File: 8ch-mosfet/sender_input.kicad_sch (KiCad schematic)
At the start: 4 parts, among them J16 Conn_01x02

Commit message: component layout looking crispy.
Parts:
- renumbered J16 to INPUT2, R102 to R101, R101 to R102
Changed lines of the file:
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@@
 		(dnp no)
 		(fields_autoplaced yes)
-		(property "Reference" "#PWR096"
+		(property "Reference" "#PWR095"
 			(at 152.4 102.87 0)
 			(effects
@@
 			(project "8ch-mosfet"
 				(path "/c83c6236-96e9-46ad-9d7a-9e2efa4a7966/96edcf10-ad2e-4b0c-9bcf-7ec233542517"
-					(reference "#PWR096")
-					(unit 1)
-				)
-				(path "/c83c6236-96e9-46ad-9d7a-9e2efa4a7966/b7d804d7-e10b-40c8-a6a0-65b4ae1f95ab"
-					(reference "#PWR093")
-					(unit 1)
-				)
-				(path "/c83c6236-96e9-46ad-9d7a-9e2efa4a7966/be792642-71a0-4d31-8160-e0873aa75416"
-					(reference "#PWR0102")
-					(unit 1)
-				)
-				(path "/c83c6236-96e9-46ad-9d7a-9e2efa4a7966/f630e7bf-424c-48d0-b4f5-b992ebe5ac06"
-					(reference "#PWR099")
+					(reference "#PWR095")
+					(unit 1)
+				)
+				(path "/c83c6236-96e9-46ad-9d7a-9e2efa4a7966/b7d804d7-e10b-40c8-a6a0-65b4ae1f95ab"
+					(reference "#PWR092")
+					(unit 1)
+				)
+				(path "/c83c6236-96e9-46ad-9d7a-9e2efa4a7966/be792642-71a0-4d31-8160-e0873aa75416"
+					(reference "#PWR0101")
+					(unit 1)
+				)
+				(path "/c83c6236-96e9-46ad-9d7a-9e2efa4a7966/f630e7bf-424c-48d0-b4f5-b992ebe5ac06"
+					(reference "#PWR098")
 					(unit 1)
 				)
@@
 		(on_board yes)
 		(dnp no)
-		(property "Reference" "#PWR097"
+		(property "Reference" "#PWR096"
 			(at 152.4 125.73 0)
 			(effects
@@
 			(project "8ch-mosfet"
 				(path "/c83c6236-96e9-46ad-9d7a-9e2efa4a7966/96edcf10-ad2e-4b0c-9bcf-7ec233542517"
-					(reference "#PWR097")
-					(unit 1)
-				)
-				(path "/c83c6236-96e9-46ad-9d7a-9e2efa4a7966/b7d804d7-e10b-40c8-a6a0-65b4ae1f95ab"
-					(reference "#PWR094")
-					(unit 1)
-				)
-				(path "/c83c6236-96e9-46ad-9d7a-9e2efa4a7966/be792642-71a0-4d31-8160-e0873aa75416"
-					(reference "#PWR0103")
-					(unit 1)
-				)
-				(path "/c83c6236-96e9-46ad-9d7a-9e2efa4a7966/f630e7bf-424c-48d0-b4f5-b992ebe5ac06"
-					(reference "#PWR0100")
+					(reference "#PWR096")
+					(unit 1)
+				)
+				(path "/c83c6236-96e9-46ad-9d7a-9e2efa4a7966/b7d804d7-e10b-40c8-a6a0-65b4ae1f95ab"
+					(reference "#PWR093")
+					(unit 1)
+				)
+				(path "/c83c6236-96e9-46ad-9d7a-9e2efa4a7966/be792642-71a0-4d31-8160-e0873aa75416"
+					(reference "#PWR0102")
+					(unit 1)
+				)
+				(path "/c83c6236-96e9-46ad-9d7a-9e2efa4a7966/f630e7bf-424c-48d0-b4f5-b992ebe5ac06"
+					(reference "#PWR099")
 					(unit 1)
 				)
@@
 		(dnp no)
 		(fields_autoplaced yes)
-		(property "Reference" "#PWR098"
+		(property "Reference" "#PWR097"
 			(at 162.56 102.87 0)
 			(effects
@@
 			(project "8ch-mosfet"
 				(path "/c83c6236-96e9-46ad-9d7a-9e2efa4a7966/96edcf10-ad2e-4b0c-9bcf-7ec233542517"
-					(reference "#PWR098")
-					(unit 1)
-				)
-				(path "/c83c6236-96e9-46ad-9d7a-9e2efa4a7966/b7d804d7-e10b-40c8-a6a0-65b4ae1f95ab"
-					(reference "#PWR095")
-					(unit 1)
-				)
-				(path "/c83c6236-96e9-46ad-9d7a-9e2efa4a7966/be792642-71a0-4d31-8160-e0873aa75416"
-					(reference "#PWR0104")
-					(unit 1)
-				)
-				(path "/c83c6236-96e9-46ad-9d7a-9e2efa4a7966/f630e7bf-424c-48d0-b4f5-b992ebe5ac06"
-					(reference "#PWR0101")
+					(reference "#PWR097")
+					(unit 1)
+				)
+				(path "/c83c6236-96e9-46ad-9d7a-9e2efa4a7966/b7d804d7-e10b-40c8-a6a0-65b4ae1f95ab"
+					(reference "#PWR094")
+					(unit 1)
+				)
+				(path "/c83c6236-96e9-46ad-9d7a-9e2efa4a7966/be792642-71a0-4d31-8160-e0873aa75416"
+					(reference "#PWR0103")
+					(unit 1)
+				)
+				(path "/c83c6236-96e9-46ad-9d7a-9e2efa4a7966/f630e7bf-424c-48d0-b4f5-b992ebe5ac06"
+					(reference "#PWR0100")
 					(unit 1)
 				)
@@
 		(dnp no)
 		(fields_autoplaced yes)
-		(property "Reference" "J16"
+		(property "Reference" "INPUT2"
 			(at 142.24 100.33 0)
 			(effects
@@
 			(project ""
 				(path "/c83c6236-96e9-46ad-9d7a-9e2efa4a7966/96edcf10-ad2e-4b0c-9bcf-7ec233542517"
-					(reference "J17")
-					(unit 1)
-				)
-				(path "/c83c6236-96e9-46ad-9d7a-9e2efa4a7966/b7d804d7-e10b-40c8-a6a0-65b4ae1f95ab"
-					(reference "J16")
-					(unit 1)
-				)
-				(path "/c83c6236-96e9-46ad-9d7a-9e2efa4a7966/be792642-71a0-4d31-8160-e0873aa75416"
-					(reference "J19")
-					(unit 1)
-				)
-				(path "/c83c6236-96e9-46ad-9d7a-9e2efa4a7966/f630e7bf-424c-48d0-b4f5-b992ebe5ac06"
-					(reference "J18")
+					(reference "INPUT2")
+					(unit 1)
+				)
+				(path "/c83c6236-96e9-46ad-9d7a-9e2efa4a7966/b7d804d7-e10b-40c8-a6a0-65b4ae1f95ab"
+					(reference "INPUT1")
+					(unit 1)
+				)
+				(path "/c83c6236-96e9-46ad-9d7a-9e2efa4a7966/be792642-71a0-4d31-8160-e0873aa75416"
+					(reference "INPUT4")
+					(unit 1)
+				)
+				(path "/c83c6236-96e9-46ad-9d7a-9e2efa4a7966/f630e7bf-424c-48d0-b4f5-b992ebe5ac06"
+					(reference "INPUT3")
 					(unit 1)
 				)
@@
 		(dnp no)
 		(fields_autoplaced yes)
-		(property "Reference" "R102"
+		(property "Reference" "R101"
 			(at 154.94 111.76 0)
 			(effects
@@
 			(project "8ch-mosfet"
 				(path "/c83c6236-96e9-46ad-9d7a-9e2efa4a7966/96edcf10-ad2e-4b0c-9bcf-7ec233542517"
-					(reference "R102")
-					(unit 1)
-				)
-				(path "/c83c6236-96e9-46ad-9d7a-9e2efa4a7966/b7d804d7-e10b-40c8-a6a0-65b4ae1f95ab"
-					(reference "R99")
-					(unit 1)
-				)
-				(path "/c83c6236-96e9-46ad-9d7a-9e2efa4a7966/be792642-71a0-4d31-8160-e0873aa75416"
-					(reference "R108")
-					(unit 1)
-				)
-				(path "/c83c6236-96e9-46ad-9d7a-9e2efa4a7966/f630e7bf-424c-48d0-b4f5-b992ebe5ac06"
-					(reference "R105")
+					(reference "R101")
+					(unit 1)
+				)
+				(path "/c83c6236-96e9-46ad-9d7a-9e2efa4a7966/b7d804d7-e10b-40c8-a6a0-65b4ae1f95ab"
+					(reference "R98")
+					(unit 1)
+				)
+				(path "/c83c6236-96e9-46ad-9d7a-9e2efa4a7966/be792642-71a0-4d31-8160-e0873aa75416"
+					(reference "R107")
+					(unit 1)
+				)
+				(path "/c83c6236-96e9-46ad-9d7a-9e2efa4a7966/f630e7bf-424c-48d0-b4f5-b992ebe5ac06"
+					(reference "R104")
 					(unit 1)
 				)
@@
 		(dnp yes)
 		(fields_autoplaced yes)
-		(property "Reference" "R101"
+		(property "Reference" "R102"
 			(at 165.1 101.6 0)
 			(effects
@@
 			(project "8ch-mosfet"
 				(path "/c83c6236-96e9-46ad-9d7a-9e2efa4a7966/96edcf10-ad2e-4b0c-9bcf-7ec233542517"
-					(reference "R101")
-					(unit 1)
-				)
-				(path "/c83c6236-96e9-46ad-9d7a-9e2efa4a7966/b7d804d7-e10b-40c8-a6a0-65b4ae1f95ab"
-					(reference "R98")
-					(unit 1)
-				)
-				(path "/c83c6236-96e9-46ad-9d7a-9e2efa4a7966/be792642-71a0-4d31-8160-e0873aa75416"
-					(reference "R107")
-					(unit 1)
-				)
-				(path "/c83c6236-96e9-46ad-9d7a-9e2efa4a7966/f630e7bf-424c-48d0-b4f5-b992ebe5ac06"
-					(reference "R104")
-					(unit 1)
-				)
+					(reference "R102")
+					(unit 1)
+				)
+				(path "/c83c6236-96e9-46ad-9d7a-9e2efa4a7966/b7d804d7-e10b-40c8-a6a0-65b4ae1f95ab"
+					(reference "R99")
+					(unit 1)
+				)
+				(path "/c83c6236-96e9-46ad-9d7a-9e2efa4a7966/be792642-71a0-4d31-8160-e0873aa75416"
+					(reference "R108")
+					(unit 1)
+				)
+				(path "/c83c6236-96e9-46ad-9d7a-9e2efa4a7966/f630e7bf-424c-48d0-b4f5-b992ebe5ac06"
+					(reference "R105")
+					(unit 1)
+				)

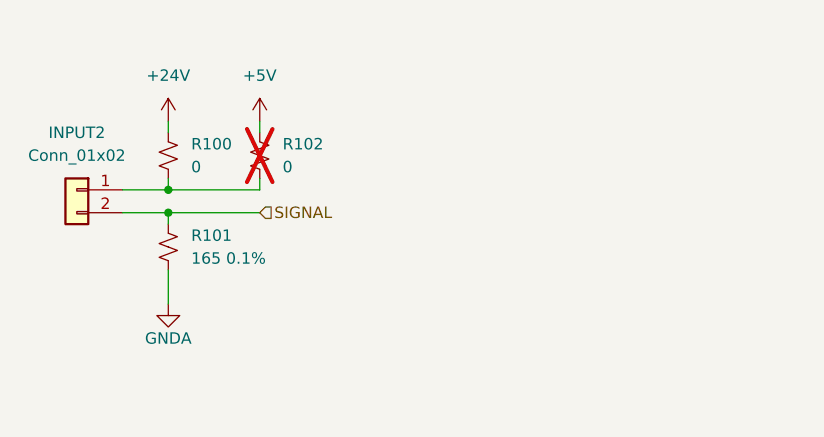
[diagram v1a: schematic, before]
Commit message: i think i figured out the tank sensors?
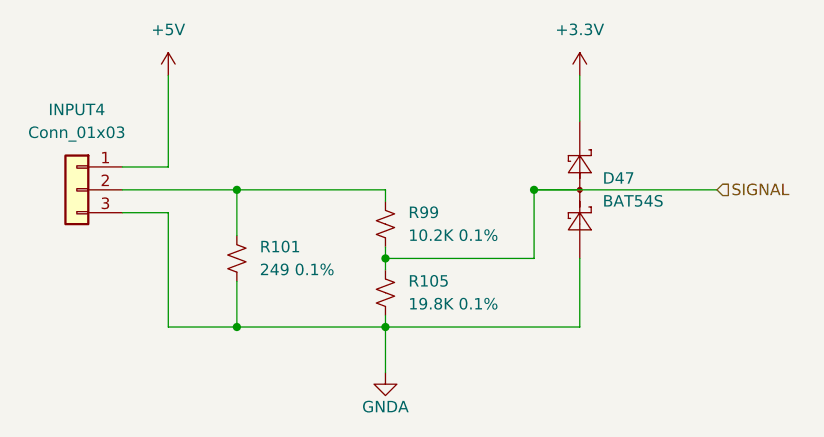
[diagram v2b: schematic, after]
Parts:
- removed INPUT2: Conn_01x02, Connector_JST:JST_PH_B2B-PH-K_1x02_P2.00mm_Vertical, symbol Connector_Generic:Conn_01x02
- removed R100, R102: 0, Resistor_SMD:R_0805_2012Metric_Pad1.20x1.40mm_HandSolder, symbol Device:R_Small_US
- added D47: BAT54S, Package_TO_SOT_SMD:SOT-23, symbol Diode:BAT54S
- added INPUT4: Conn_01x03, Connector_JST:JST_PH_B3B-PH-K_1x03_P2.00mm_Vertical, symbol Connector_Generic:Conn_01x03
- added R105: 19.8K 0.1%, Resistor_SMD:R_0805_2012Metric_Pad1.20x1.40mm_HandSolder, symbol Device:R_Small_US
- added R99: 10.2K 0.1%, Resistor_SMD:R_0805_2012Metric_Pad1.20x1.40mm_HandSolder, symbol Device:R_Small_US
- R101: value 165 0.1% -> 249 0.1%
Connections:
- net +5V: now also INPUT4.1 (Pin_1)
- net GNDA: now also D47.1 (A), INPUT4.3 (Pin_3), R105.1
- net SIGNAL: now also D47.3 (COM), R105.2, R99.1; no longer R101.2
- new net: INPUT4.2 (Pin_2), R101.2, R99.2
- new net +3.3V: D47.2 (K)
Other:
- moved on the sheet: R101
